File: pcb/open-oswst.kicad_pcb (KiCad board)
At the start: 2 copper layers, 70 x 50 mm, 16 parts

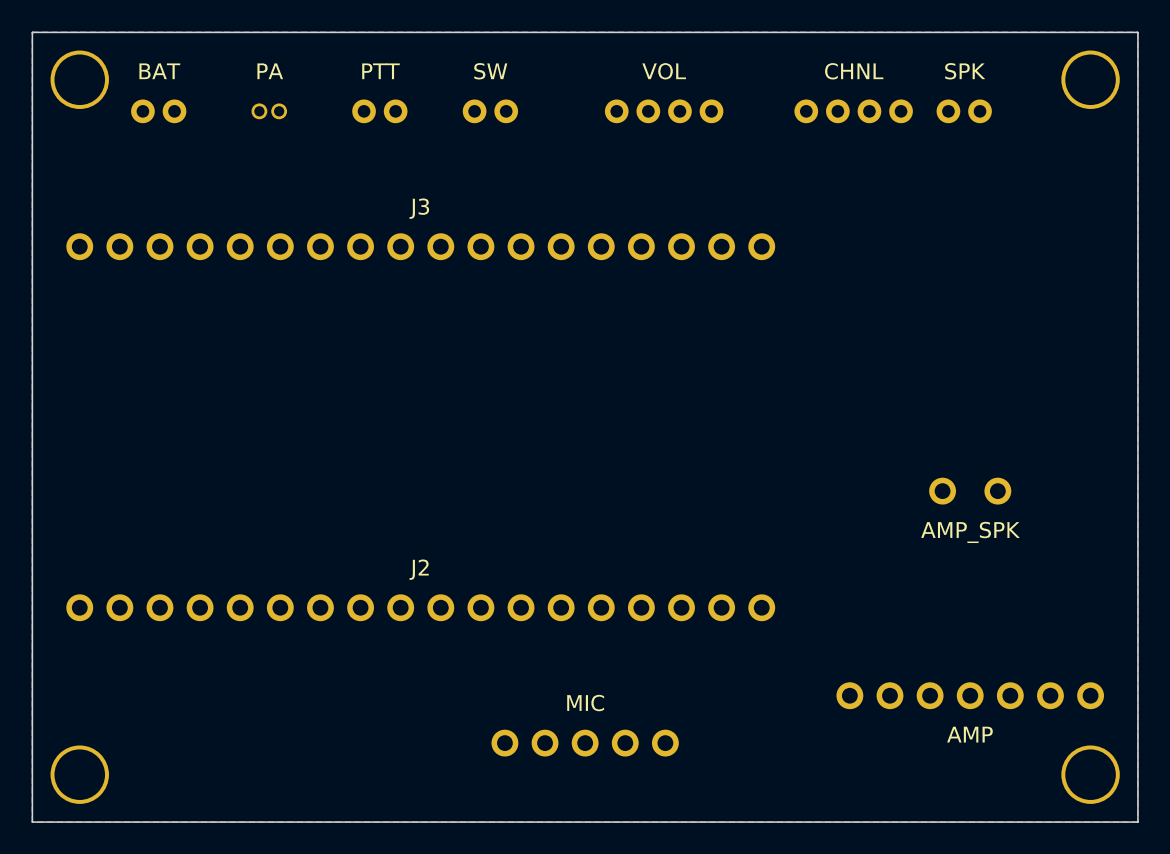
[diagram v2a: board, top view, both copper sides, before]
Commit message: PCB: use M2 mounting holes (2.2mm drill)
Co-Authored-By: Claude Opus 4.6 <noreply@anthropic.com>
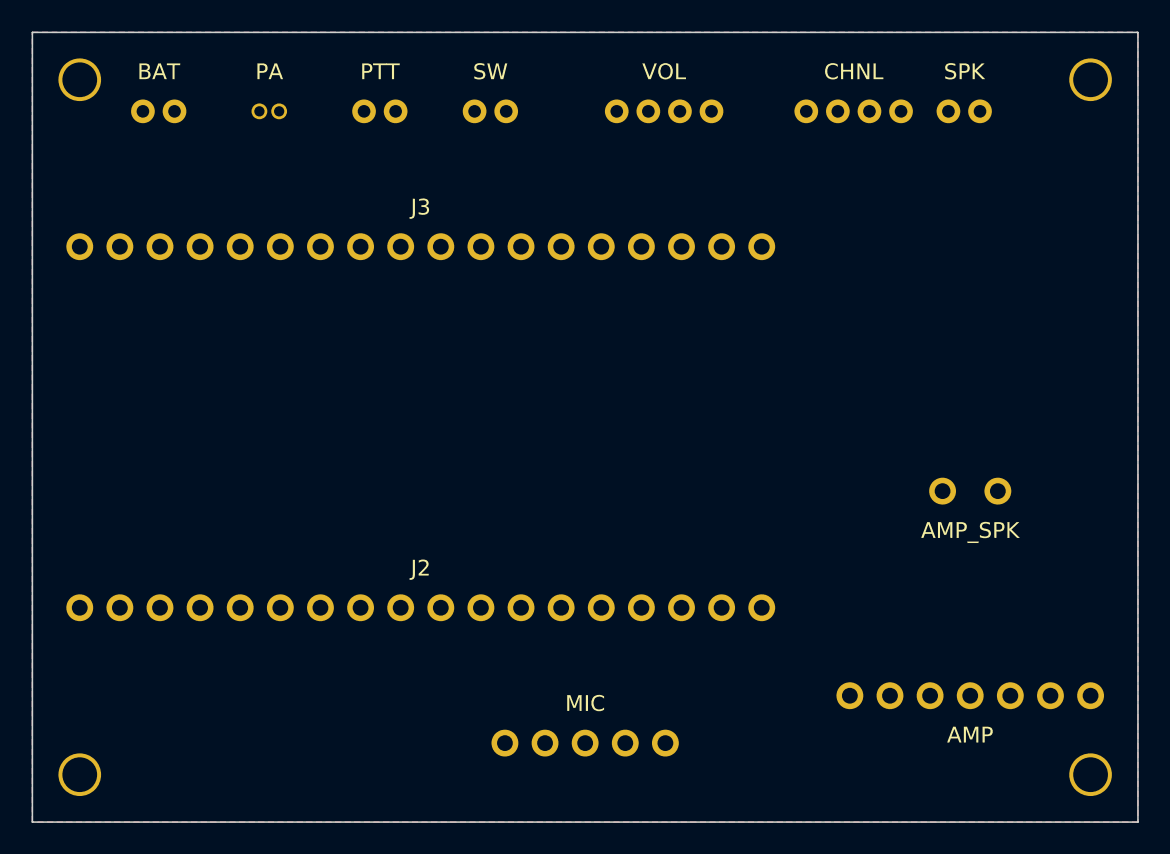
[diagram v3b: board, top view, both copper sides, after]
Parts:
- H1, H2, H3, H4: footprint MountingHole_3.2mm -> MountingHole_2.2mm
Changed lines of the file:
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@@
   )
   (gr_rect (start 113 113) (end 183 163) (stroke (width 0.1) (type solid)) (fill none) (layer "Edge.Cuts"))
-  (footprint "MountingHole_3.2mm"
+  (footprint "MountingHole_2.2mm"
     (layer "F.Cu")
     (at 116 116)
@@
     (pad "" np_thru_hole circle
       (at 0 0)
-      (size 3.7 3.7)
-      (drill 3.2)
+      (size 2.7 2.7)
+      (drill 2.2)
       (layers *.Cu *.Mask)
     )
   )
-  (footprint "MountingHole_3.2mm"
+  (footprint "MountingHole_2.2mm"
     (layer "F.Cu")
     (at 116 160)
@@
     (pad "" np_thru_hole circle
       (at 0 0)
-      (size 3.7 3.7)
-      (drill 3.2)
+      (size 2.7 2.7)
+      (drill 2.2)
       (layers *.Cu *.Mask)
     )
   )
-  (footprint "MountingHole_3.2mm"
+  (footprint "MountingHole_2.2mm"
     (layer "F.Cu")
     (at 180 116)
@@
     (pad "" np_thru_hole circle
       (at 0 0)
-      (size 3.7 3.7)
-      (drill 3.2)
+      (size 2.7 2.7)
+      (drill 2.2)
       (layers *.Cu *.Mask)
     )
   )
-  (footprint "MountingHole_3.2mm"
+  (footprint "MountingHole_2.2mm"
     (layer "F.Cu")
     (at 180 160)
@@
     (pad "" np_thru_hole circle
       (at 0 0)
-      (size 3.7 3.7)
-      (drill 3.2)
+      (size 2.7 2.7)
+      (drill 2.2)
       (layers *.Cu *.Mask)
     )

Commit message: PCB: add silkscreen text, USLetter paper, M2 holes
- Add project name + git SHA to front silkscreen
- Fix paper size to USLetter for 1:1 printing
- Add add_text() method to PCB DSL

Co-Authored-By: Claude Opus 4.6 <noreply@anthropic.com>
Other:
- board text added: "open-oswst 6aa8376"
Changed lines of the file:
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@@
     (legacy_teardrops no)
   )
-  (paper "A4")
+  (paper "USLetter")
   (layers
     (0 "F.Cu" signal)
@@
   )
   (gr_rect (start 113 113) (end 183 163) (stroke (width 0.1) (type solid)) (fill none) (layer "Edge.Cuts"))
+  (gr_text "open-oswst  6aa8376"
+    (at 148.0 161)
+    (layer "F.SilkS")
+    (effects (font (size 0.8 0.8) (thickness 0.12)))
+  )
   (footprint "MountingHole_2.2mm"
     (layer "F.Cu")

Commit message: PCB: reorder top-edge connectors (BAT SW PA PTT VOL CHNL SPK)
Co-Authored-By: Claude Opus 4.6 <noreply@anthropic.com>
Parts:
- moved SW 14.0 mm to (128.0, 118.0)
- moved PA 7.00 mm to (135.0, 118.0)
- moved PTT 7.00 mm to (142.0, 118.0)
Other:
- board text added: "open-oswst cd7cb5c"
- board text removed: "open-oswst 6aa8376"
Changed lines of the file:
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@@
   )
   (gr_rect (start 113 113) (end 183 163) (stroke (width 0.1) (type solid)) (fill none) (layer "Edge.Cuts"))
-  (gr_text "open-oswst  6aa8376"
+  (gr_text "open-oswst  cd7cb5c"
     (at 148.0 161)
     (layer "F.SilkS")
@@
     )
   )
+  (footprint "JST_PH_B2B"
+    (layer "F.Cu")
+    (at 128 118)
+    (fp_text reference "SW" (at 0 -2.5) (layer "F.SilkS")
+      (effects (font (size 1 1) (thickness 0.15)))
+    )
+    (pad "1" thru_hole circle
+      (at -1.0 0)
+      (size 1.5 1.5)
+      (drill 0.8)
+      (layers *.Cu *.Mask)
+      (net 1 "VBAT")
+    )
+    (pad "2" thru_hole circle
+      (at 1.0 0)
+      (size 1.5 1.5)
+      (drill 0.8)
+      (layers *.Cu *.Mask)
+      (net 3 "VSW")
+    )
+  )
   (footprint "JST_SH_B2B"
     (layer "F.Cu")
-    (at 128 118)
+    (at 135 118)
     (fp_text reference "PA" (at 0 -2.5) (layer "F.SilkS")
       (effects (font (size 1 1) (thickness 0.15)))
@@
   (footprint "JST_PH_B2B"
     (layer "F.Cu")
-    (at 135 118)
+    (at 142 118)
     (fp_text reference "PTT" (at 0 -2.5) (layer "F.SilkS")
       (effects (font (size 1 1) (thickness 0.15)))
@@
     )
   )
-  (footprint "JST_PH_B2B"
-    (layer "F.Cu")
-    (at 142 118)
-    (fp_text reference "SW" (at 0 -2.5) (layer "F.SilkS")
-      (effects (font (size 1 1) (thickness 0.15)))
-    )
-    (pad "1" thru_hole circle
-      (at -1.0 0)
-      (size 1.5 1.5)
-      (drill 0.8)
-      (layers *.Cu *.Mask)
-      (net 1 "VBAT")
-    )
-    (pad "2" thru_hole circle
-      (at 1.0 0)
-      (size 1.5 1.5)
-      (drill 0.8)
-      (layers *.Cu *.Mask)
-      (net 3 "VSW")
-    )
-  )

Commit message: PCB: fix connector types to match actual parts
- BAT: JST-PH → JST-SH (1.25mm) to match battery connector
- PA: JST-SH → JST-PH (2.0mm) for JST-PH cable
- SPK: JST-PH → JST-ZH (1.5mm) to match speaker connector
- Flip SPK pin order to uncross traces
- Add add_jst_zh() to PCB DSL

Co-Authored-By: Claude Opus 4.6 <noreply@anthropic.com>
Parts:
- removed the BAT at (121.0, 118.0)
- removed the PA at (135.0, 118.0)
- removed the SPK at (172.0, 118.0)
- added BAT: , JST_SH_B2B, F.Cu at (121.0, 118.0)
- added PA: , JST_PH_B2B, F.Cu at (135.0, 118.0)
- added SPK: , JST_ZH_B2B, F.Cu at (172.0, 118.0)
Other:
- board text added: "open-oswst 796951d"
- board text removed: "open-oswst cd7cb5c"
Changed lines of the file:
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@@
   (net 9 "CHNL_B")
   (net 10 "CHNL_SW")
-  (net 11 "SPK+")
-  (net 12 "SPK-")
+  (net 11 "SPK-")
+  (net 12 "SPK+")
   (net 13 "3V3")
   (net 14 "MIC_OUT")
@@
   )
   (gr_rect (start 113 113) (end 183 163) (stroke (width 0.1) (type solid)) (fill none) (layer "Edge.Cuts"))
-  (gr_text "open-oswst  cd7cb5c"
+  (gr_text "open-oswst  796951d"
     (at 148.0 161)
     (layer "F.SilkS")
@@
     )
   )
-  (footprint "JST_PH_B2B"
+  (footprint "JST_SH_B2B"
     (layer "F.Cu")
     (at 121 118)
     (fp_text reference "BAT" (at 0 -2.5) (layer "F.SilkS")
-      (effects (font (size 1 1) (thickness 0.15)))
-    )
-    (pad "+" thru_hole circle
-      (at -1.0 0)
-      (size 1.5 1.5)
-      (drill 0.8)
-      (layers *.Cu *.Mask)
-      (net 1 "VBAT")
-    )
-    (pad "-" thru_hole circle
-      (at 1.0 0)
-      (size 1.5 1.5)
-      (drill 0.8)
-      (layers *.Cu *.Mask)
-      (net 2 "GND")
-    )
-  )
-  (footprint "JST_PH_B2B"
-    (layer "F.Cu")
-    (at 128 118)
-    (fp_text reference "SW" (at 0 -2.5) (layer "F.SilkS")
-      (effects (font (size 1 1) (thickness 0.15)))
-    )
-    (pad "1" thru_hole circle
-      (at -1.0 0)
-      (size 1.5 1.5)
-      (drill 0.8)
-      (layers *.Cu *.Mask)
-      (net 1 "VBAT")
-    )
-    (pad "2" thru_hole circle
-      (at 1.0 0)
-      (size 1.5 1.5)
-      (drill 0.8)
-      (layers *.Cu *.Mask)
-      (net 3 "VSW")
-    )
-  )
-  (footprint "JST_SH_B2B"
-    (layer "F.Cu")
-    (at 135 118)
-    (fp_text reference "PA" (at 0 -2.5) (layer "F.SilkS")
       (effects (font (size 1 1) (thickness 0.15)))
     )
@@
       (drill 0.65)
       (layers *.Cu *.Mask)
-      (net 3 "VSW")
+      (net 1 "VBAT")
     )
     (pad "-" thru_hole circle
@@
   (footprint "JST_PH_B2B"
     (layer "F.Cu")
+    (at 128 118)
+    (fp_text reference "SW" (at 0 -2.5) (layer "F.SilkS")
+      (effects (font (size 1 1) (thickness 0.15)))
+    )
+    (pad "1" thru_hole circle
+      (at -1.0 0)
+      (size 1.5 1.5)
+      (drill 0.8)
+      (layers *.Cu *.Mask)
+      (net 1 "VBAT")
+    )
+    (pad "2" thru_hole circle
+      (at 1.0 0)
+      (size 1.5 1.5)
+      (drill 0.8)
+      (layers *.Cu *.Mask)
+      (net 3 "VSW")
+    )
+  )
+  (footprint "JST_PH_B2B"
+    (layer "F.Cu")
+    (at 135 118)
+    (fp_text reference "PA" (at 0 -2.5) (layer "F.SilkS")
+      (effects (font (size 1 1) (thickness 0.15)))
+    )
+    (pad "+" thru_hole circle
+      (at -1.0 0)
+      (size 1.5 1.5)
+      (drill 0.8)
+      (layers *.Cu *.Mask)
+      (net 3 "VSW")
+    )
+    (pad "-" thru_hole circle
+      (at 1.0 0)
+      (size 1.5 1.5)
+      (drill 0.8)
+      (layers *.Cu *.Mask)
+      (net 2 "GND")
+    )
+  )
+  (footprint "JST_PH_B2B"
+    (layer "F.Cu")
     (at 142 118)
     (fp_text reference "PTT" (at 0 -2.5) (layer "F.SilkS")
@@
     )
   )
-  (footprint "JST_PH_B2B"
+  (footprint "JST_ZH_B2B"
     (layer "F.Cu")
     (at 172 118)
@@
       (effects (font (size 1 1) (thickness 0.15)))
     )
+    (pad "-" thru_hole circle
+      (at -0.75 0)
+      (size 1.1 1.1)
+      (drill 0.7)
+      (layers *.Cu *.Mask)
+      (net 11 "SPK-")
+    )
     (pad "+" thru_hole circle
-      (at -1.0 0)
-      (size 1.5 1.5)
-      (drill 0.8)
-      (layers *.Cu *.Mask)
-      (net 11 "SPK+")
-    )
-    (pad "-" thru_hole circle
-      (at 1.0 0)
-      (size 1.5 1.5)
-      (drill 0.8)
-      (layers *.Cu *.Mask)
-      (net 12 "SPK-")
+      (at 0.75 0)
+      (size 1.1 1.1)
+      (drill 0.7)
+      (layers *.Cu *.Mask)
+      (net 12 "SPK+")
     )
   )
@@
       (drill 1.0)
       (layers *.Cu *.Mask)
-      (net 11 "SPK+")
+      (net 12 "SPK+")
     )
     (pad "-" thru_hole circle
@@
       (drill 1.0)
       (layers *.Cu *.Mask)
-      (net 12 "SPK-")
-    )
-  )
+      (net 11 "SPK-")
+    )
+  )
